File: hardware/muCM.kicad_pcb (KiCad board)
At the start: 4 copper layers, 32 x 18 mm, 88 parts, among them J1 CDM806-04A-MP-F011-67, J2 USB4105, J3 CDM805-08A-FP-F011-67, J4 UF.L, Q1 2N7002KL3A-TP, Q2 40 MHz, SW3 NO, SW4 NO, U1 FUSB302B01MPX, U2 TCAN3413DRBR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

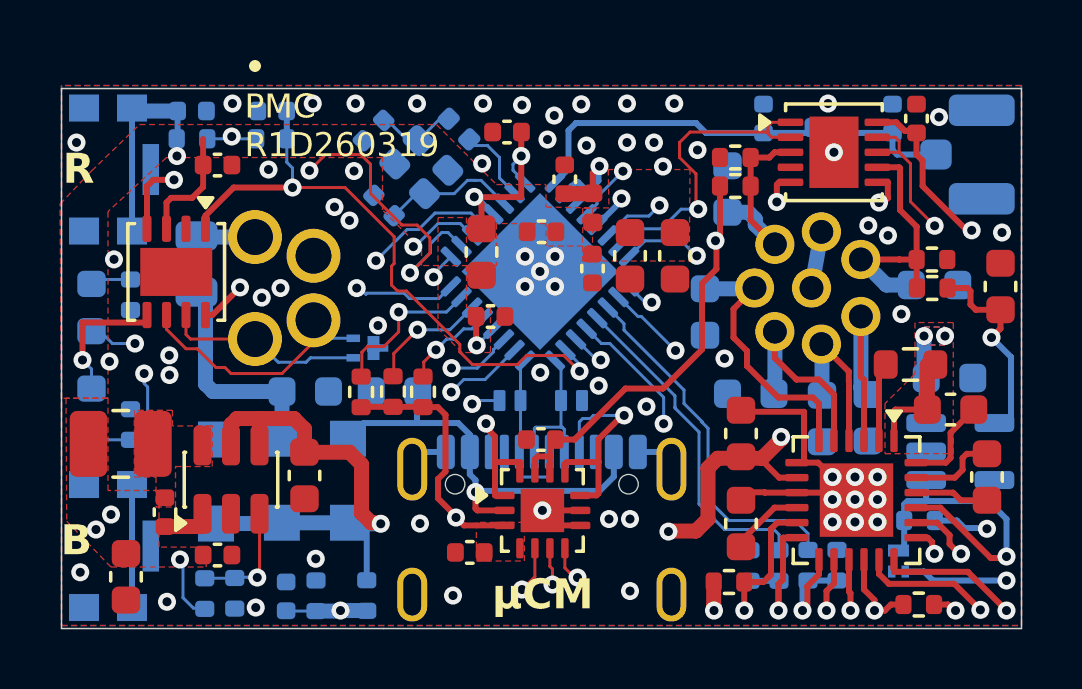
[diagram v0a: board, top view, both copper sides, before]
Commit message: finished single board layout - upping to panel size
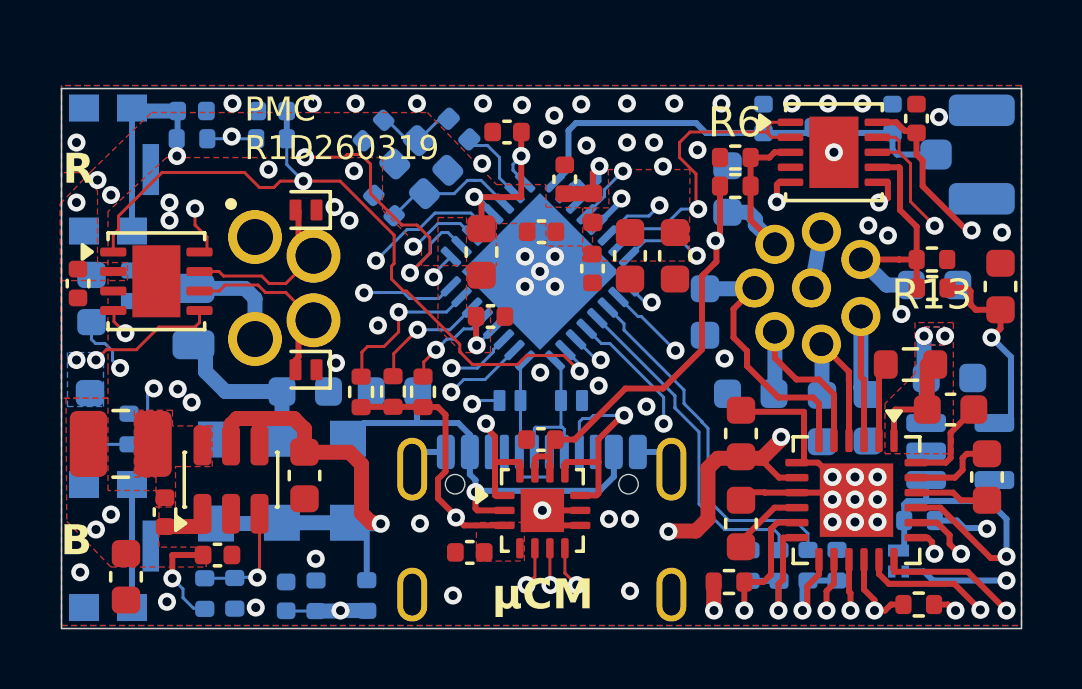
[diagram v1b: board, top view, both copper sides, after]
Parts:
- added D7: PESD1CANFD36L-QYL, Diode_SMD:D_SOD-882, F.Cu at (117.2, 87.2)
- D1: value ESDCAN03 -> PESD1CANFD36L-QYL; footprint PCM_PartyWagon112_DFN:DFN1006-3 -> Diode_SMD:D_SOD-882; moved to F.Cu
- R13, R6: footprint PCM_SparkFun-Resistor:R_0402_1005Metric -> Resistor_SMD:R_0402_1005Metric
- moved C13 6.10 mm to (109.5, 84.3), turned to -90 degrees
- moved D1 5.04 mm to (117.2, 81.8), turned to 180 degrees
- moved F1 1.75 mm to (113.4, 85.4)
- moved U2 0.73 mm to (112.2, 84.2), turned to 0 degrees
- moved LED3 0.30 mm to (110.0, 84.8)
- moved R21 0.30 mm to (111.3, 84.4)
- moved R3 0.16 mm to (111.2, 89.2)
- moved LED1 0.16 mm to (110.0, 88.7)
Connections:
- D1 pad 1: /CAN+ -> GND
- D1 pad 2: /CAN- -> /CAN+
- J1 pad 1: /VDC_IN -> GND
- J1 pad 2: GND -> /CAN+
- J1 pad 3: /CAN+ -> /VDC_IN
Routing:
- net /MCU/BOOT/CANTX: track 38.7 -> 45.1 mm
- net /MCU/CANRX: track 17.8 -> 22.0 mm
- net /SLEEP: track 59.3 -> 56.4 mm
- net /CAN-: track 8.72 -> 6.27 mm
- net +3V3: track 90.9 -> 88.9 mm, vias 14 -> 17
- net /VDC_F: track 7.42 -> 5.47 mm
- net /VDC_IN: track 1.97 -> 3.54 mm
- net /VMEAS_IN: track 43.8 -> 45.1 mm
- net /MCU/LED0: track 17.8 -> 18.7 mm
- net GND: track 26.9 -> 26.1 mm, vias 65 -> 68
- net /CAN+: track 6.67 -> 6.15 mm
- added copper zone on B.Cu, net +3V3

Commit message: Added stencils and other stuff i guess - should commit more regularly
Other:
- board text added: "PMC R1D260326"
- board text removed: "PMC R1D260319"
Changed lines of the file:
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@@
 			(at 0 -1.17 0)
 			(layer "F.SilkS")
+			(hide yes)
 			(effects
 				(font
@@
 			(at 0 -1.17 180)
 			(layer "F.SilkS")
+			(hide yes)
 			(effects
 				(font
@@
 		(layer "Edge.Cuts")
 	)
-	(gr_text "PMC\nR1D260319"
+	(gr_text "PMC\nR1D260326"
 		(at 115.1 80.25 0)
 		(layer "F.SilkS")
@@
 	)
 	(segment
-		(start 130.178849 83.398999)
-		(end 130.025 83.552848)
-		(width 0.1)
-		(layer "In1.Cu")
-		(net 31)
-	)
-	(segment
 		(start 131.528612 80.575)
 		(end 136.721388 80.575)
@@
 			)
 		)
+	)
+	(zone
+		(net 0)
+		(net_name "")
+		(layer "F.Cu")
+		(hatch edge 0.5)
+		(connect_pads
+			(clearance 0)
+		)
+		(min_thickness 0.25)
+		(filled_areas_thickness no)
+		(keepout
+			(tracks allowed)
+			(vias allowed)
+			(pads allowed)
+			(copperpour not_allowed)
+			(footprints allowed)
+		)
+		(placement
+			(enabled no)
+			(sheetname "/")
+		)
+		(fill
+			(thermal_gap 0.5)
+			(thermal_bridge_width 0.5)
+		)
+		(polygon
+			(pts
+				(xy 130.6 86) (xy 131.2 86) (xy 131.2 85.6) (xy 130.6 85.6)
+			)
+		)
